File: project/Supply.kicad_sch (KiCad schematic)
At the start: 20 parts, among them IC11 TL7702A, M1 R-785.0-1.0, SW6 FT232 RESET, SW7 RESET, X7 GND, X8 DC IN

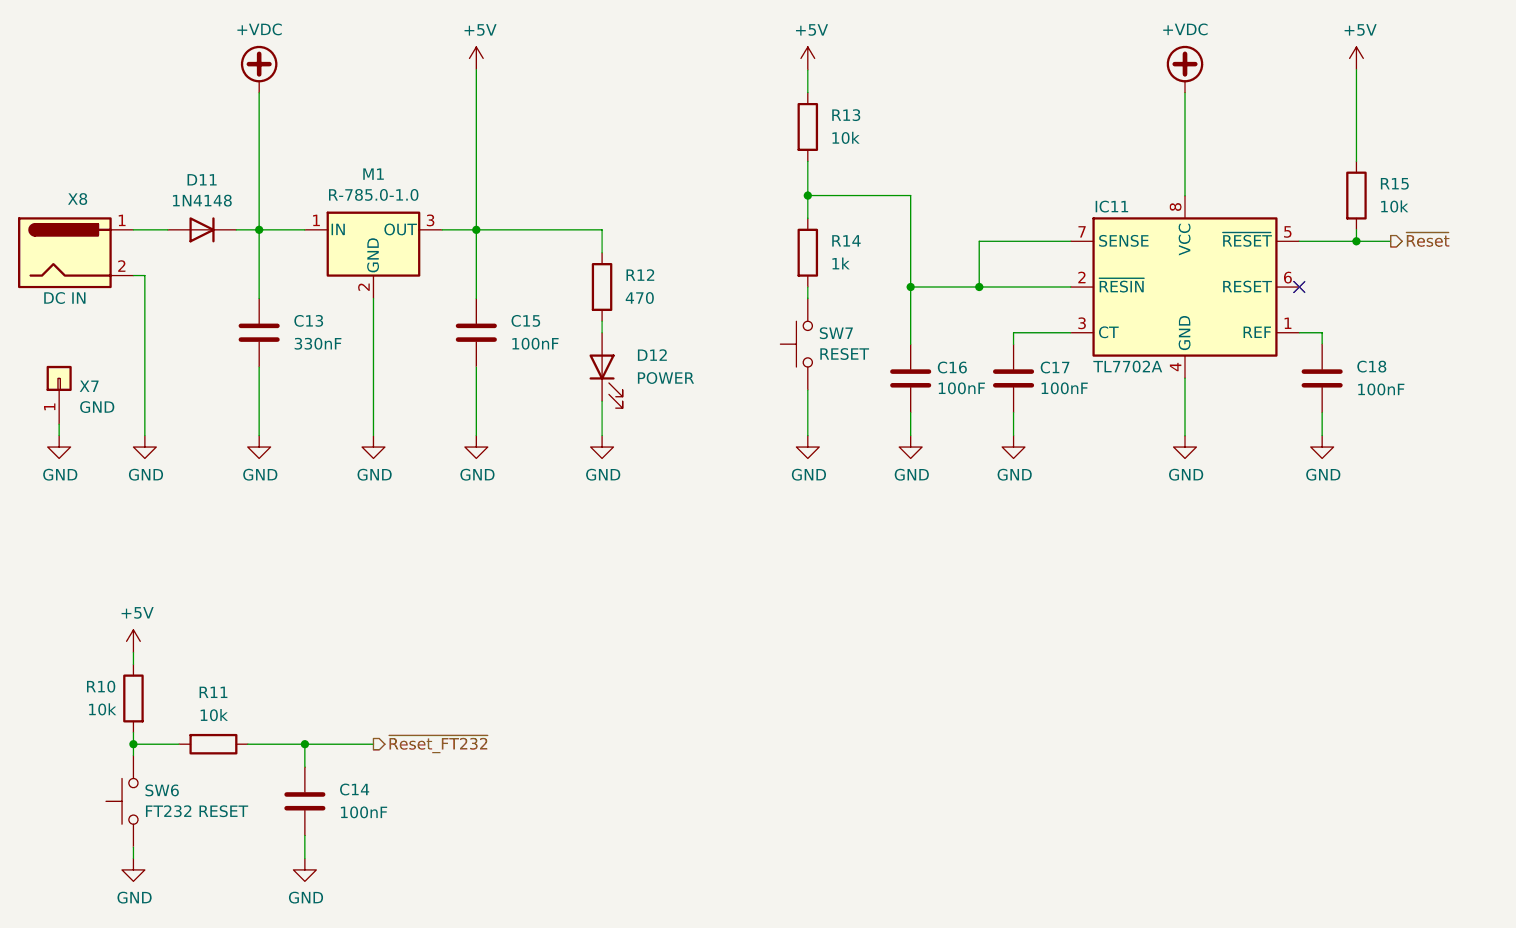
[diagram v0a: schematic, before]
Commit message: Fix grid issues, fix missing libraries, replace FT232 with FT231
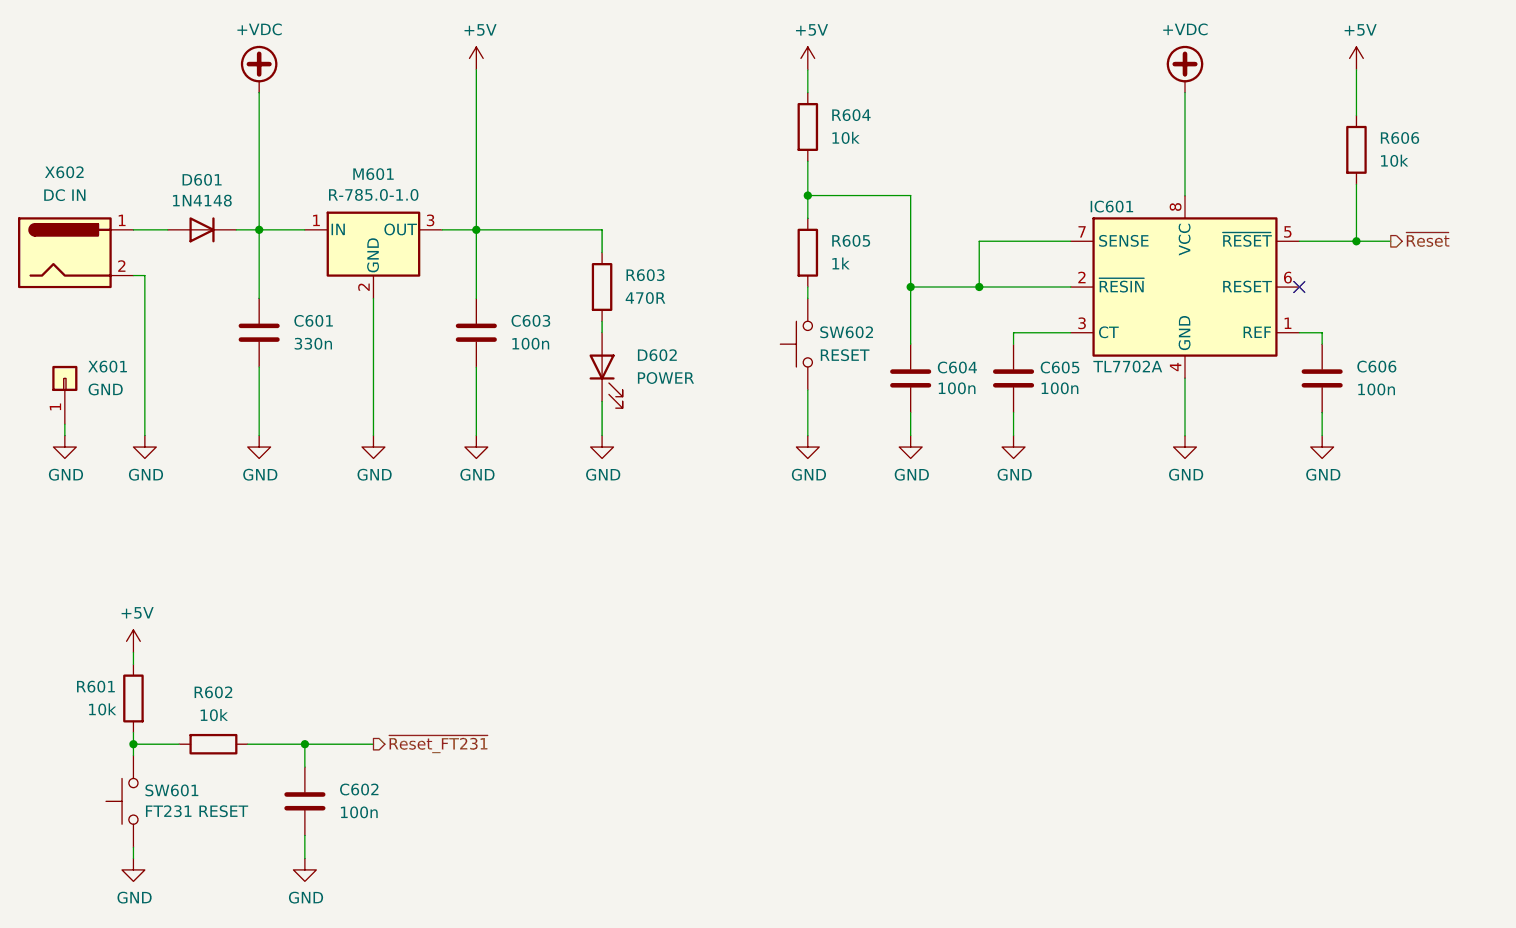
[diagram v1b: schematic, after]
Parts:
- C601: renamed from C13; value 330nF -> 330n
- C602: renamed from C14; value 100nF -> 100n
- C603: renamed from C15; value 100nF -> 100n
- C604: renamed from C16; value 100nF -> 100n
- C605: renamed from C17; value 100nF -> 100n
- C606: renamed from C18; value 100nF -> 100n
- D601: renamed from D11; footprint Diode_THT:D_DO-35_SOD27_P7.62mm_Horizontal -> Diode_SMD:D_SOD-123
- R603: renamed from R12; value 470 -> 470R
- SW601: renamed from SW6; value FT232 RESET -> FT231 RESET
- X602: renamed from X8; footprint Connector_Generic:BarrelJack_Wuerth_6941xx301002 -> Connector_BarrelJack:BarrelJack_Wuerth_6941xx301002
- renumbered D12 to D602, IC11 to IC601, M1 to M601, R10 to R601, R11 to R602, R13 to R604, R14 to R605, R15 to R606, SW7 to SW602, X7 to X601
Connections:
- net ~{Reset_FT232} renamed ~{Reset_FT231}
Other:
- moved on the sheet: R606, X601

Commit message: Fix swapped DM and DP, add missing datasheets, remove Mouser property
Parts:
- C601: Mouser 581-SR205E334MARTR1 -> (none)
- C602, C603, C604, C605, C606: Mouser 810-FA18X8R1H104KRU6 -> (none)
- D601: Mouser 512-1N4148 -> (none)
- D602: Mouser 941-C503BRANCZ0C0AA1 -> (none)
- IC601: Mouser 595-TL7702ACP -> (none)
- M601: Mouser 919-R-785.0-1.0 -> (none)
- R601, R602, R604, R606: Mouser 603-MFP-25BRD52-10K -> (none)
- R603: Mouser 603-MFP-25BRD52-470R -> (none)
- R605: Mouser 603-MFP-25BRD52-1K -> (none)
- SW601, SW602: Mouser 506-2-1825910-7 -> (none)
- X601: Mfr. No. 4-103327-3 -> 5-146281-1; Mouser 571-4-103327-3 -> (none)
- X602: Mouser 710-694106301002 -> (none)
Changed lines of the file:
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@@
 			)
 		)
-		(property "Datasheet" "~"
+		(property "Datasheet" "https://www.mouser.de/datasheet/2/723/HB_C503B_RAS_RAN_AAS_AAN_RBS_RBN_ABS_ABN_RCS_RCN_A-3402026.pdf"
 			(at 120.65 110.49 0)
 			(effects
@@
 			)
 		)
-		(property "Mouser" "941-C503BRANCZ0C0AA1"
-			(at 120.65 110.49 0)
-			(effects
-				(font
-					(size 1.27 1.27)
-				)
-				(hide yes)
-			)
-		)
 		(property "Distributor" "Mouser"
 			(at 120.65 110.49 0)
@@
 			)
 		)
-		(property "Datasheet" "~"
+		(property "Datasheet" "https://www.mouser.de/datasheet/2/447/Yageo_LR_MFP_1-1947926.pdf"
 			(at 120.65 101.6 0)
 			(effects
@@
 			)
 		)
-		(property "Mouser" "603-MFP-25BRD52-470R"
-			(at 120.65 101.6 0)
-			(effects
-				(font
-					(size 1.27 1.27)
-				)
-				(hide yes)
-			)
-		)
 		(property "Distributor" "Mouser"
 			(at 120.65 101.6 0)
@@
 			)
 		)
-		(property "Mouser" "710-694106301002"
-			(at 60.96 97.79 0)
-			(effects
-				(font
-					(size 1.27 1.27)
-				)
-				(hide yes)
-			)
-		)
 		(property "Distributor" "Mouser"
 			(at 60.96 97.79 0)
@@
 			)
 		)
-		(property "Datasheet" "~"
+		(property "Datasheet" "https://www.mouser.de/datasheet/2/447/YAGEO_MFP_datasheet_2024v3-3447153.pdf"
 			(at 204.47 86.36 0)
 			(effects
@@
 			)
 		)
-		(property "Mouser" "603-MFP-25BRD52-10K"
-			(at 204.47 86.36 0)
-			(effects
-				(font
-					(size 1.27 1.27)
-				)
-				(hide yes)
-			)
-		)
 		(property "Distributor" "Mouser"
 			(at 204.47 86.36 0)
@@
 			)
 		)
-		(property "Datasheet" "~"
+		(property "Datasheet" "https://www.mouser.de/datasheet/2/418/9/ENG_CD_146281_G4-2007824.pdf"
 			(at 60.96 111.76 0)
 			(effects
@@
 			)
 		)
-		(property "Mfr. No." "4-103327-3"
-			(at 60.96 111.76 0)
-			(effects
-				(font
-					(size 1.27 1.27)
-				)
-				(hide yes)
-			)
-		)
-		(property "Mouser" "571-4-103327-3"
+		(property "Mfr. No." "5-146281-1"
 			(at 60.96 111.76 0)
 			(effects
@@
 			)
 		)
-		(property "Datasheet" "~"
+		(property "Datasheet" "https://www.mouser.de/datasheet/2/447/YAGEO_MFP_datasheet_2024v3-3447153.pdf"
 			(at 68.58 147.32 0)
 			(effects
@@
 			)
 		)
-		(property "Mouser" "603-MFP-25BRD52-10K"
-			(at 68.58 147.32 0)
-			(effects
-				(font
-					(size 1.27 1.27)
-				)
-				(hide yes)
-			)
-		)
 		(property "Distributor" "Mouser"
 			(at 68.58 147.32 0)
@@
 			)
 		)
-		(property "Datasheet" "~"
+		(property "Datasheet" "https://product.tdk.com/system/files/dam/doc/product/capacitor/ceramic/lead-mlcc/catalog/leadmlcc_halogenfree_fa150_en.pdf?ref_disty=mouser"
 			(at 87.63 158.75 0)
 			(effects
@@
 			)
 		)
-		(property "Mouser" "810-FA18X8R1H104KRU6"
-			(at 87.63 158.75 0)
-			(effects
-				(font
-					(size 1.27 1.27)
-				)
-				(hide yes)
-			)
-		)
 		(property "Distributor" "Mouser"
 			(at 87.63 158.75 0)
@@
 			)
 		)
-		(property "Datasheet" "~"
+		(property "Datasheet" "https://www.mouser.de/datasheet/2/418/7/ENG_CD_1825910_C10-2021098.pdf"
 			(at 63.5 158.75 0)
 			(effects
@@
 			)
 		)
-		(property "Mouser" "506-2-1825910-7"
-			(at 68.58 158.75 0)
-			(effects
-				(font
-					(size 1.27 1.27)
-				)
-				(hide yes)
-			)
-		)
 		(property "Distributor" "Mouser"
 			(at 68.58 158.75 0)
@@
 			)
 		)
-		(property "Datasheet" "~"
+		(property "Datasheet" "https://www.mouser.de/datasheet/2/447/Yageo_LR_MFP_1-1947926.pdf"
 			(at 143.51 97.79 0)
 			(effects
@@
 			)
 		)
-		(property "Mouser" "603-MFP-25BRD52-1K"
-			(at 143.51 97.79 0)
-			(effects
-				(font
-					(size 1.27 1.27)
-				)
-				(hide yes)
-			)
-		)
 		(property "Distributor" "Mouser"
 			(at 143.51 97.79 0)
@@
 			)
 		)
-		(property "Datasheet" "~"
+		(property "Datasheet" "https://www.mouser.de/datasheet/2/447/YAGEO_MFP_datasheet_2024v3-3447153.pdf"
 			(at 77.47 152.4 0)
 			(effects
@@
 			)
 		)
-		(property "Mouser" "603-MFP-25BRD52-10K"
-			(at 77.47 152.4 0)
-			(effects
-				(font
-					(size 1.27 1.27)
-				)
-				(hide yes)
-			)
-		)
 		(property "Distributor" "Mouser"
 			(at 77.47 152.4 0)
@@
 			)
 		)
-		(property "Datasheet" "~"
+		(property "Datasheet" "https://www.mouser.de/datasheet/2/447/YAGEO_MFP_datasheet_2024v3-3447153.pdf"
 			(at 143.51 83.82 0)
 			(effects
@@
 			)
 		)
-		(property "Mouser" "603-MFP-25BRD52-10K"
-			(at 143.51 83.82 0)
-			(effects
-				(font
-					(size 1.27 1.27)
-				)
-				(hide yes)
-			)
-		)
 		(property "Distributor" "Mouser"
 			(at 143.51 83.82 0)
@@
 			)
 		)
-		(property "Datasheet" "~"
+		(property "Datasheet" "https://www.mouser.de/datasheet/2/418/7/ENG_CD_1825910_C10-2021098.pdf"
 			(at 138.43 107.95 0)
 			(effects
@@
 			)
 		)
-		(property "Mouser" "506-2-1825910-7"
-			(at 143.51 107.95 0)
-			(effects
-				(font
-					(size 1.27 1.27)
-				)
-				(hide yes)
-			)
-		)
 		(property "Distributor" "Mouser"
 			(at 143.51 107.95 0)
@@
 			)
 		)
-		(property "Datasheet" "~"
+		(property "Datasheet" "https://product.tdk.com/system/files/dam/doc/product/capacitor/ceramic/lead-mlcc/catalog/leadmlcc_halogenfree_fa150_en.pdf?ref_disty=mouser"
 			(at 154.94 111.76 0)
 			(effects
@@
 			)
 		)
-		(property "Mouser" "810-FA18X8R1H104KRU6"
-			(at 154.94 111.76 0)
-			(effects
-				(font
-					(size 1.27 1.27)
-				)
-				(hide yes)
-			)
-		)
 		(property "Distributor" "Mouser"
 			(at 154.94 111.76 0)
@@
 			)
 		)
-		(property "Datasheet" "~"
+		(property "Datasheet" "https://www.mouser.de/datasheet/2/40/SR_Series-3165337.pdf"
 			(at 82.55 106.68 0)
 			(effects
@@
 			)
 		)
-		(property "Mouser" "581-SR205E334MARTR1"
-			(at 82.55 106.68 0)
-			(effects
-				(font
-					(size 1.27 1.27)
-				)
-				(hide yes)
-			)
-		)
 		(property "Distributor" "Mouser"
 			(at 82.55 106.68 0)
@@
 			)
 		)
-		(property "Datasheet" "~"
+		(property "Datasheet" "https://product.tdk.com/system/files/dam/doc/product/capacitor/ceramic/lead-mlcc/catalog/leadmlcc_halogenfree_fa150_en.pdf?ref_disty=mouser"
 			(at 106.68 106.68 0)
 			(effects
@@
 			)
 		)
-		(property "Mouser" "810-FA18X8R1H104KRU6"
-			(at 106.68 106.68 0)
-			(effects
-				(font
-					(size 1.27 1.27)
-				)
-				(hide yes)
-			)
-		)
 		(property "Distributor" "Mouser"
 			(at 106.68 106.68 0)
@@
 			)
 		)
-		(property "Mouser" "512-1N4148"
-			(at 76.2 95.25 0)
-			(effects
-				(font
-					(size 1.27 1.27)
-				)
-				(hide yes)
-			)
-		)
 		(property "Distributor" "Mouser"
 			(at 76.2 95.25 0)
@@
 			)
 		)
-		(property "Mouser" "919-R-785.0-1.0"
-			(at 95.25 95.25 0)
-			(effects
-				(font
-					(size 1.27 1.27)
-				)
-				(hide yes)
-			)
-		)
 		(property "Mfr. No." "R-785.0-1.0"
 			(at 95.25 95.25 0)
@@
 			)
 		)
-		(property "Datasheet" "~"
+		(property "Datasheet" "https://product.tdk.com/system/files/dam/doc/product/capacitor/ceramic/lead-mlcc/catalog/leadmlcc_halogenfree_fa150_en.pdf?ref_disty=mouser"
 			(at 166.37 111.76 0)
 			(effects
@@
 			)
 		)
-		(property "Mouser" "810-FA18X8R1H104KRU6"
-			(at 166.37 111.76 0)
-			(effects
-				(font
-					(size 1.27 1.27)
-				)
-				(hide yes)
-			)
-		)
 		(property "Distributor" "Mouser"
 			(at 166.37 111.76 0)
@@
 			)
 		)
-		(property "Datasheet" "~"
+		(property "Datasheet" "https://product.tdk.com/system/files/dam/doc/product/capacitor/ceramic/lead-mlcc/catalog/leadmlcc_halogenfree_fa150_en.pdf?ref_disty=mouser"
 			(at 200.66 111.76 0)
 			(effects
@@
 			)
 		)
-		(property "Mouser" "810-FA18X8R1H104KRU6"
-			(at 200.66 111.76 0)
-			(effects
-				(font
-					(size 1.27 1.27)
-				)
-				(hide yes)
-			)
-		)
 		(property "Distributor" "Mouser"
 			(at 200.66 111.76 0)
@@
 			(at 185.42 101.6 0)
 			(effects
-				(font
-					(size 1.27 1.27)
-				)
-				(hide yes)
-			)
-		)
-		(property "Mouser" "595-TL7702ACP"
-			(at 185.42 101.6 0)
-			(effects
